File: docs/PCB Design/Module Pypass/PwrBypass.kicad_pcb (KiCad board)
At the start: 4 copper layers, 25.9 x 62.3 mm, 5 parts, among them J11 Conn_02x05_Top_Bottom, J14 Conn_02x04_Counter_Clockwise

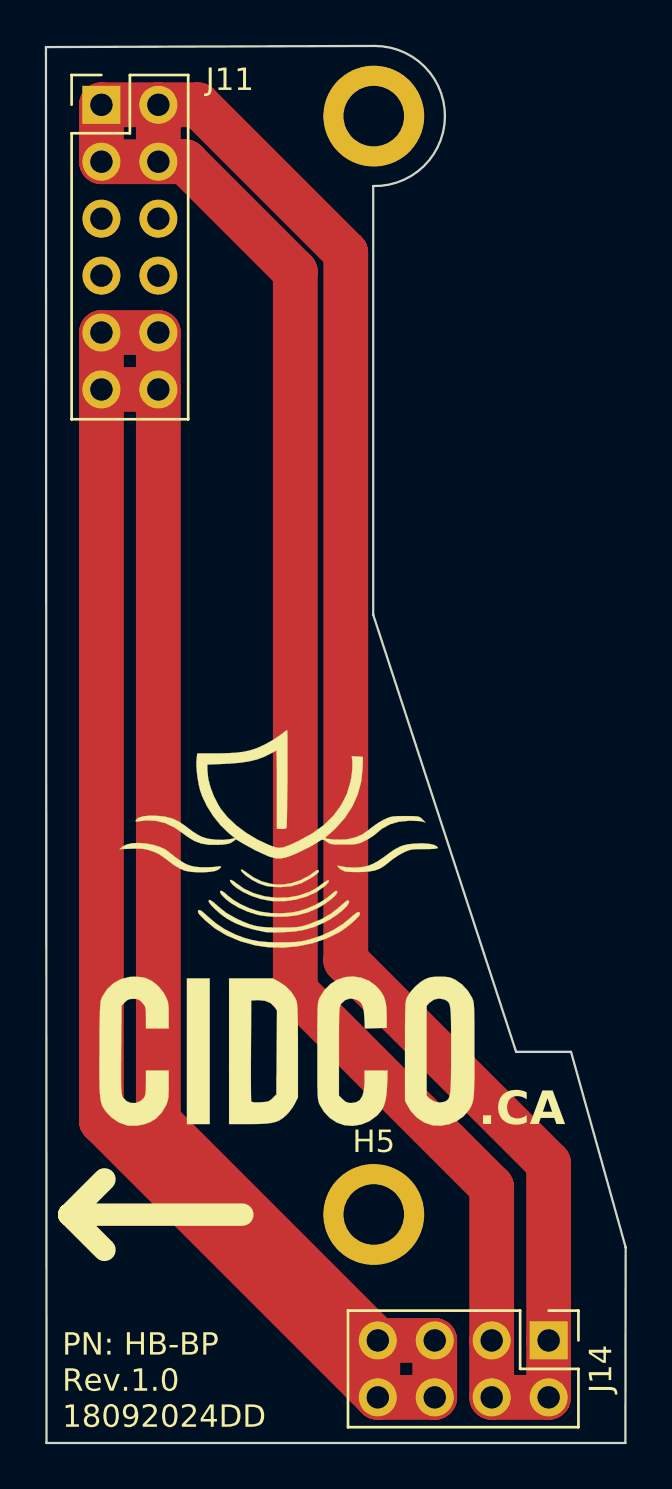
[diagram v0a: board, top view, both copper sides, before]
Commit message: module power 1.0 module bypass 1.1
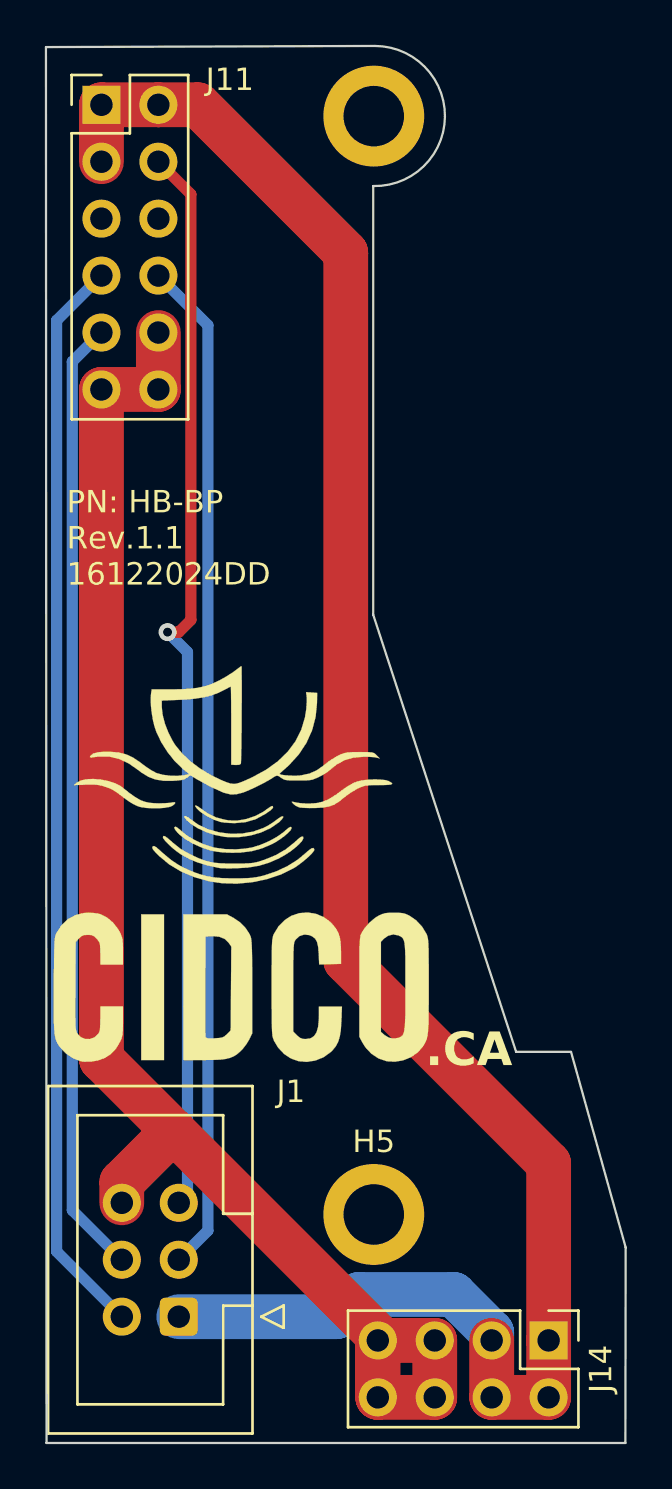
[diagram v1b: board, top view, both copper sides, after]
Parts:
- added J1: Conn_02x03_Top_Bottom, Connector_IDC:IDC-Header_2x03_P2.54mm_Vertical, F.Cu at (107.5, 97.0)
- moved logo1 3.51 mm to (110.5, 76.5)
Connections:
- J11 pad 1: +5V -> VCC
- J11 pad 2: +5V -> VCC
- J11 pad 3: +5V -> VCC
- J11 pad 4: +5V -> Signal
- J11 pad 7: unconnected-(J11-Pin_7-Pad7) -> Red
- J11 pad 8: unconnected-(J11-Pin_8-Pad8) -> Green
- J11 pad 9: GND -> Blue
- J14 pad 1: +5V -> VCC
- J14 pad 2: +5V -> VCC
- J14 pad 3: +5V -> VCC
- J14 pad 4: +5V -> VCC
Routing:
- net +5V: track 140.6 -> 0.00 mm
- net VCC: track 0.00 -> 91.5 mm
- net Red: track 0.00 -> 48.5 mm
- net Signal: track 0.00 -> 48.3 mm, vias 0 -> 1
- net GND: track 116.9 -> 69.5 mm
- net Green: track 0.00 -> 45.4 mm
- net Blue: track 0.00 -> 42.8 mm
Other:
- copper layers 4 -> 2
- board text added: "PN: HB-BP Rev.1.1 16122024DD"
- board text removed: "PN: HB-BP Rev.1.0 18092024DD"
